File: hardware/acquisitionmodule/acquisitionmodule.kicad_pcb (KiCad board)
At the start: 2 copper layers, 57.8 x 38.1 mm, 11 parts, among them J1 Conn_Coaxial, J2 USB_B_Mini, J3 Conn_Coaxial, U1 LM358, U2 LM358

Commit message: changes in prive libs
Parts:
- added C3: C, Capacitors_SMD:C_0805_HandSoldering, B.Cu at (152.8, 110.8)
- added REF**: MountingHole_3.5mm_Pad, Mounting_Holes:MountingHole_3.5mm_Pad, F.Cu at (175.0, 85.0)
- added REF**: MountingHole_3.5mm_Pad, Mounting_Holes:MountingHole_3.5mm_Pad, F.Cu at (175.0, 115.0)
- added REF**: MountingHole_3.5mm_Pad, Mounting_Holes:MountingHole_3.5mm_Pad, F.Cu at (115.0, 115.0)
- added REF**: MountingHole_3.5mm_Pad, Mounting_Holes:MountingHole_3.5mm_Pad, F.Cu at (115.0, 85.0)
- C1, C2, R1, R2, R3, R4: moved to B.Cu
- J2: value USB_B_Mini -> AVR-ISP-6; footprint Connectors:USB_Mini-B -> Pin_Headers:Pin_Header_Straight_2x03_Pitch2.54mm
- J3: value Conn_Coaxial -> USB_B_Mini; footprint Connectors:bnc-ci -> Connectors:USB_Mini-B
- U1: value LM358 -> ADS1110; footprint TO_SOT_Packages_SMD:SOT-23-8 -> IonizationChamber:ADS1110; moved to B.Cu
- U2: value LM358 -> ATtiny88-AU; footprint TO_SOT_Packages_SMD:SOT-23-8 -> Housings_QFP:LQFP-32_7x7mm_Pitch0.8mm; moved to B.Cu
- moved J3 50.5 mm to (115.6, 99.7)
- moved C2 39.7 mm to (140.7, 85.9)
- moved R4 37.6 mm to (140.8, 87.7)
- moved R3 35.8 mm to (140.8, 89.6)
- moved U2 32.0 mm to (130.2, 87.6)
- moved C1 14.9 mm to (142.6, 94.3)
- moved U1 13.3 mm to (147.4, 108.4)
- moved J1 9.89 mm to (170.0, 100.0)
- moved R2 6.75 mm to (155.4, 105.1)
- moved R1 4.67 mm to (141.5, 104.1)
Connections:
- C2 pad 1: Net-(C2-Pad1) -> VCC
- J2 pad 1: (no net) -> Net-(J2-Pad1)
- J2 pad 2: (no net) -> VCC
- J2 pad 4: (no net) -> Net-(J2-Pad4)
- J2 pad 5: (no net) -> Net-(J2-Pad5)
- J2 pad 6: Net-(J2-Pad6) -> GND
- J3 pad 1: Net-(J3-Pad1) -> VCC
- J3 pad 2: GND -> (no net)
- R3 pad 1: Net-(J3-Pad1) -> VCC
- R3 pad 2: GND -> Net-(R3-Pad2)
- R4 pad 1: Net-(C2-Pad1) -> Net-(R3-Pad2)
- R4 pad 2: Net-(J3-Pad1) -> GND
- U1 pad 1: (no net) -> Net-(C1-Pad1)
- U1 pad 2: (no net) -> GND
- U1 pad 3: (no net) -> Net-(U1-Pad3)
- U1 pad 4: (no net) -> Net-(U1-Pad4)
- U1 pad 5: (no net) -> VCC
- U1 pad 6: (no net) -> Net-(R3-Pad2)
- U2 pad 5: (no net) -> Net-(U2-Pad21)
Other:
- board size 57.8 x 38.1 mm -> 70 x 40 mm

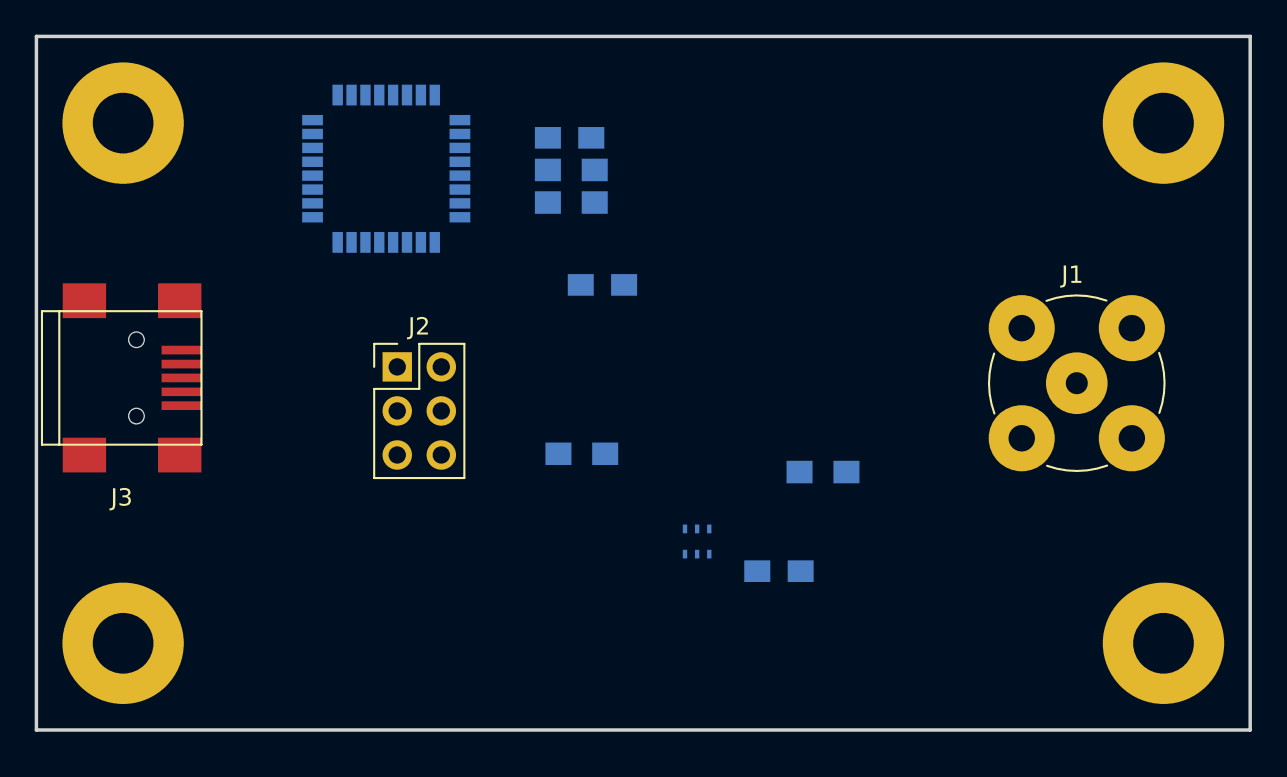
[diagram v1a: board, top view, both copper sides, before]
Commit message: tlv700 footprint added
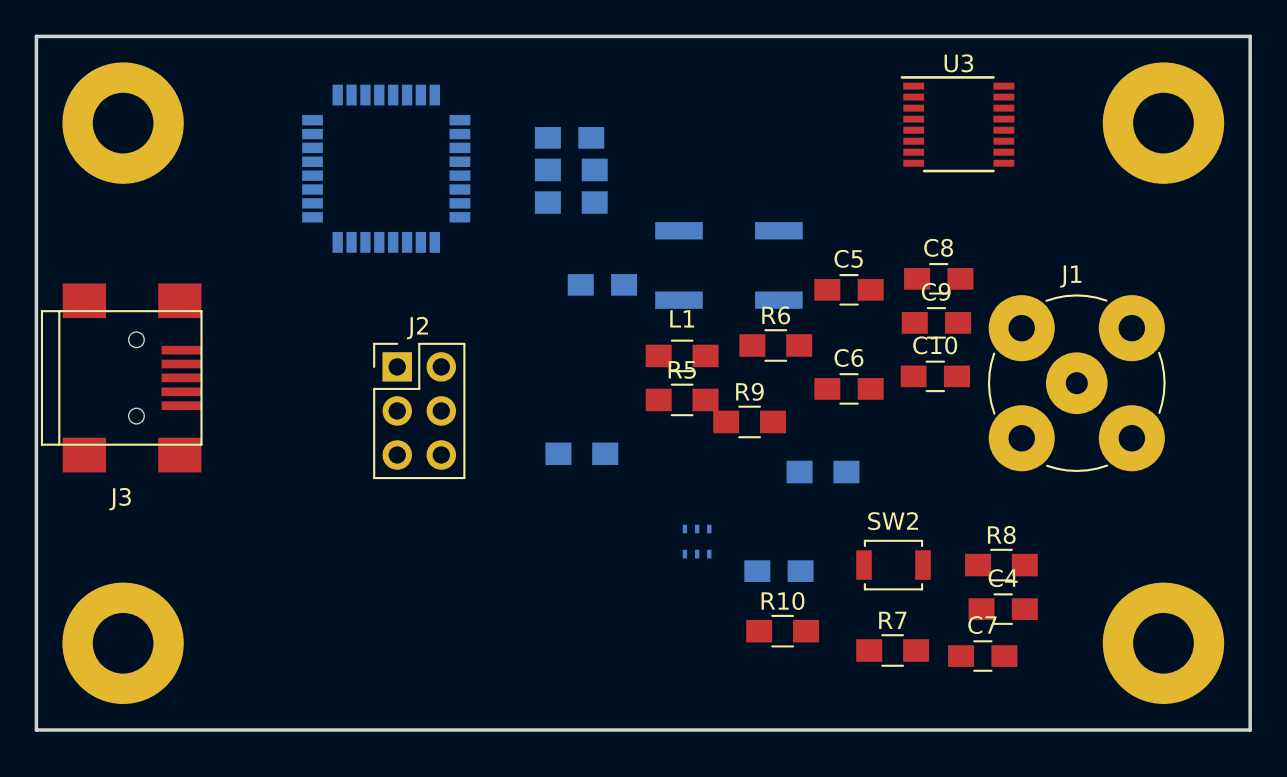
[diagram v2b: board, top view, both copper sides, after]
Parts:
- added C10: C, Capacitors_SMD:C_0805_HandSoldering, F.Cu at (161.8, 99.6)
- added C4: 47p, Capacitors_SMD:C_0805_HandSoldering, F.Cu at (165.8, 113.0)
- added C5: 47p, Capacitors_SMD:C_0805_HandSoldering, F.Cu at (156.9, 94.6)
- added C6: 100n, Capacitors_SMD:C_0805_HandSoldering, F.Cu at (156.9, 100.3)
- added C7: 100n, Capacitors_SMD:C_0805_HandSoldering, F.Cu at (164.6, 115.7)
- added C8: 100n, Capacitors_SMD:C_0805_HandSoldering, F.Cu at (162.0, 94.0)
- added C9: 100n, Capacitors_SMD:C_0805_HandSoldering, F.Cu at (161.9, 96.5)
- added L1: L_Core_Ferrite, Inductors_SMD:L_0805_HandSoldering, F.Cu at (147.2, 98.4)
- added R10: 1k, Resistors_SMD:R_0805_HandSoldering, F.Cu at (153.0, 114.3)
- added R5: 22R, Resistors_SMD:R_0805_HandSoldering, F.Cu at (147.2, 101.0)
- added R6: 22R, Resistors_SMD:R_0805_HandSoldering, F.Cu at (152.6, 97.8)
- added R7: 1k, Resistors_SMD:R_0805_HandSoldering, F.Cu at (159.4, 115.4)
- added R8: 1k, Resistors_SMD:R_0805_HandSoldering, F.Cu at (165.7, 110.5)
- added R9: 1k, Resistors_SMD:R_0805_HandSoldering, F.Cu at (151.1, 102.2)
- added SW1: SW_Push, Buttons_Switches_SMD:SW_SPST_B3SL-1022P, B.Cu at (149.9, 93.2)
- added SW2: SW_Push, Buttons_Switches_SMD:SW_SPST_B3U-1000P, F.Cu at (159.4, 110.5)
- added U3: FT201XS, Housings_SSOP:SSOP-16_3.9x4.9mm_Pitch0.635mm, F.Cu at (163.2, 85.1)
- C3: value C -> 100n
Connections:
- net Net-(U1-Pad4) renamed /SDA
- J2 pad 3: (no net) -> Net-(J2-Pad3)
- J3 pad 1: VCC -> Net-(C7-Pad1)
- J3 pad 2: (no net) -> Net-(C4-Pad1)
- J3 pad 3: (no net) -> Net-(C5-Pad1)
- J3 pad 4: (no net) -> GND
- U1 pad 3: Net-(U1-Pad3) -> (no net)
- U2 pad 17: (no net) -> Net-(J2-Pad3)
- U2 pad 21: Net-(U2-Pad21) -> GND
- U2 pad 28: Net-(U1-Pad3) -> /SCL
- U2 pad 4: (no net) -> VCC
- U2 pad 5: Net-(U2-Pad21) -> GND
